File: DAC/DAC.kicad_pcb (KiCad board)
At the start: 4 copper layers, 54 x 21.6 mm, 32 parts, among them J1 Conn_01x06, J2 Conn_01x06, U1 TPS73633DBV, U2 PCM5242RHB

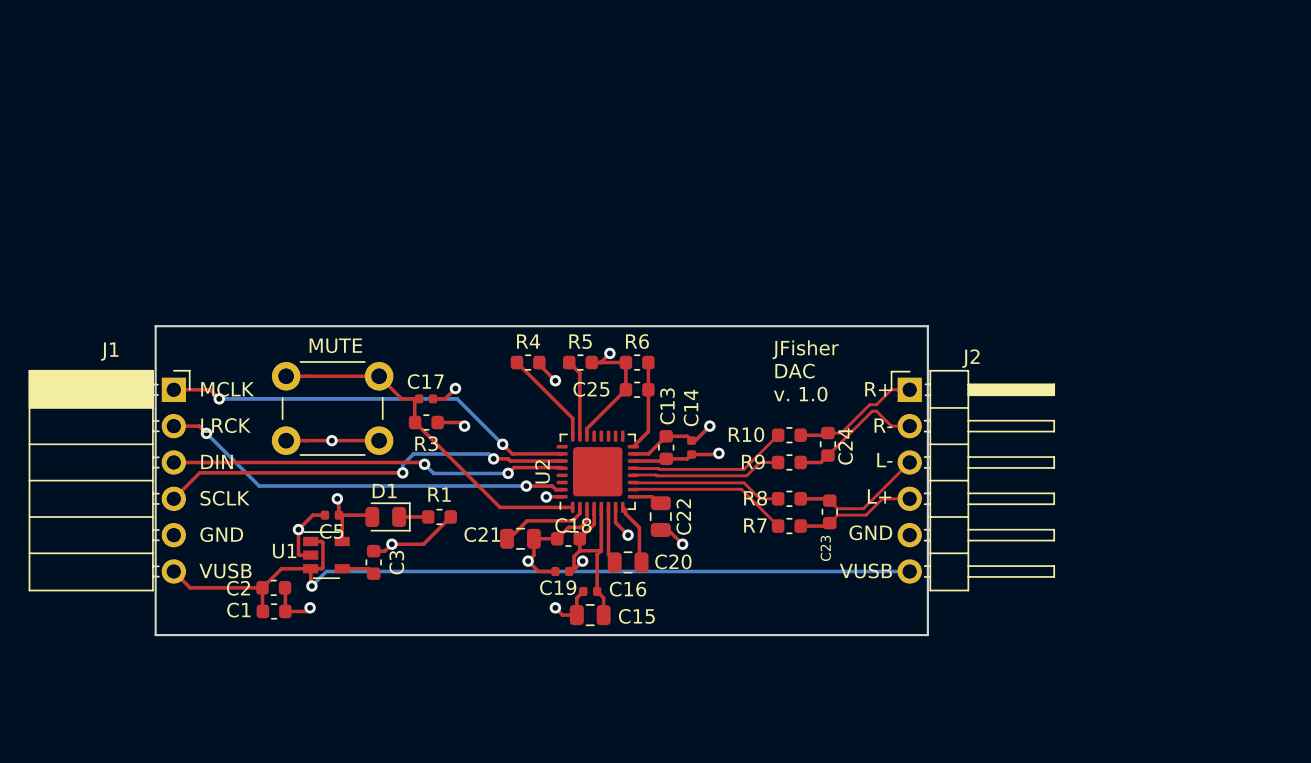
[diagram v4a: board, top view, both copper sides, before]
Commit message: Update DAC to expose config pins and to use larger components
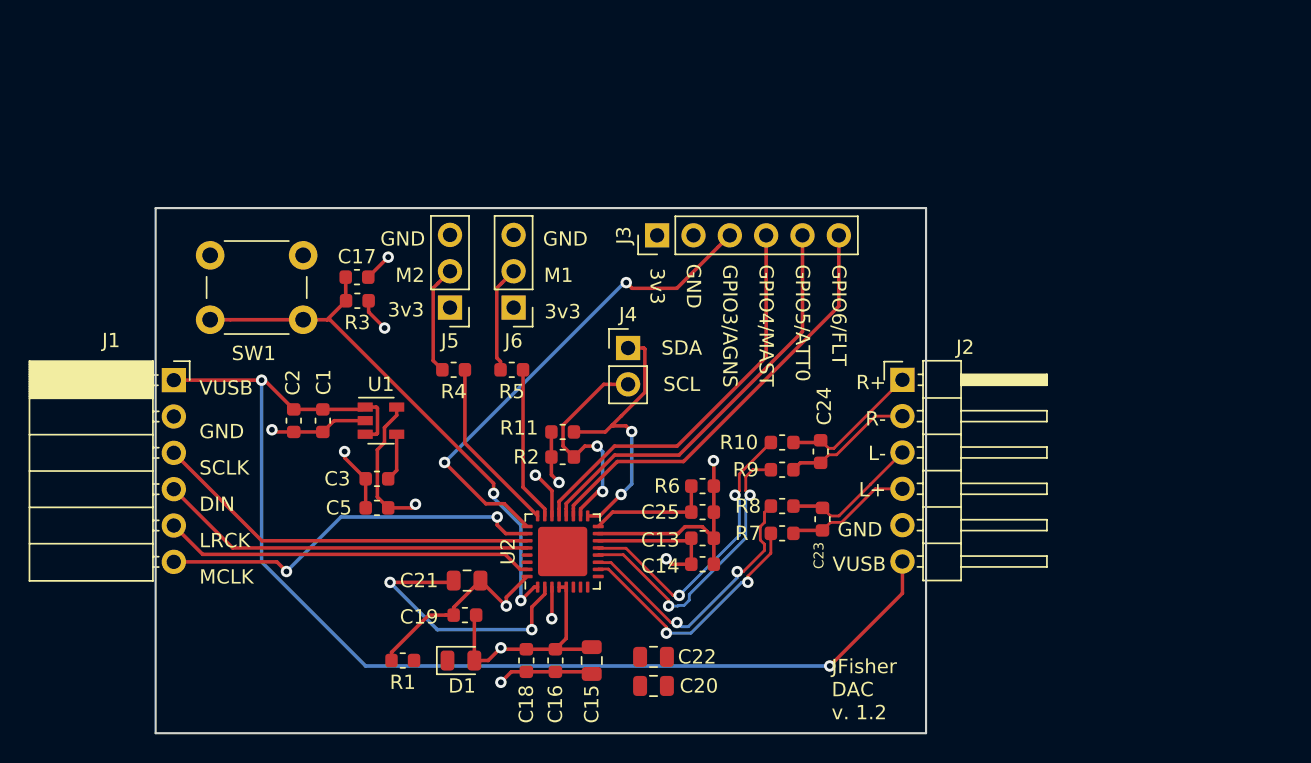
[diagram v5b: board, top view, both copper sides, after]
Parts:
- removed MUTE: SW_Push, Button_Switch_THT:SW_PUSH_6mm
- added J3: Conn_01x06_Male, Connector_PinHeader_2.54mm:PinHeader_1x06_P2.54mm_Vertical, F.Cu at (146.8, 34.3)
- added J4: Conn_01x02, Connector_PinHeader_2.54mm:PinHeader_1x02_P2.54mm_Vertical, F.Cu at (144.8, 42.2)
- added J5: Conn_01x03_Male, Connector_PinHeader_2.54mm:PinHeader_1x03_P2.54mm_Vertical, F.Cu at (132.3, 39.3)
- added J6: Conn_01x03_Male, Connector_PinHeader_2.54mm:PinHeader_1x03_P2.54mm_Vertical, F.Cu at (136.8, 39.3)
- added R11: 4.7k, Resistor_SMD:R_0603_1608Metric, F.Cu at (140.2, 48.0)
- added R2: 4.7k, Resistor_SMD:R_0603_1608Metric, F.Cu at (140.2, 49.8)
- added SW1: SW_Push, Button_Switch_THT:SW_PUSH_6mm, F.Cu at (115.6, 35.7)
- C14, C16, C17, C19, C5: footprint Capacitor_SMD:C_0402_1005Metric -> Capacitor_SMD:C_0603_1608Metric
- moved C1 13.8 mm to (123.4, 47.2), turned to 270 degrees
- moved C2 11.8 mm to (121.4, 47.2), turned to 270 degrees
- moved D1 11.3 mm to (133.1, 64.0), turned to 0 degrees
- moved R1 10.4 mm to (129.0, 64.0), turned to 180 degrees
- moved U1 10.1 mm to (127.5, 47.2)
- moved C22 9.82 mm to (146.6, 63.8), turned to 0 degrees
- moved C17 9.78 mm to (125.8, 37.2)
- moved R3 9.78 mm to (125.9, 38.9)
- moved R6 9.77 mm to (150.0, 51.8), turned to 180 degrees
- moved C25 9.70 mm to (150.0, 53.6), turned to 0 degrees
- moved C18 9.00 mm to (137.7, 64.0), turned to 270 degrees
- moved C20 8.82 mm to (146.6, 65.8)
- moved C14 8.19 mm to (150.0, 57.3), turned to 0 degrees
- moved C19 7.46 mm to (133.4, 60.8)
- moved C13 6.82 mm to (150.0, 55.5), turned to 0 degrees
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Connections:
- net Net-(R4-Pad1) renamed MODE2
- net Net-(R5-Pad1) renamed MODE1
- J1 pad 1: I2S_MCLK -> VUSB
- J1 pad 2: I2S_LRCK -> GND
- J1 pad 3: I2S_DIN -> I2S_SCLK
- J1 pad 4: I2S_SCLK -> I2S_DIN
- J1 pad 5: GND -> I2S_LRCK
- J1 pad 6: VUSB -> I2S_MCLK
- R4 pad 2: +3V3 -> Net-(J5-Pad2)
- R5 pad 2: GND -> Net-(J6-Pad2)
- U2 pad 17: (no net) -> SDA_MOSI_ATT2
- U2 pad 18: (no net) -> SCL_MC_ATT1
- U2 pad 19: (no net) -> GPIO5_ATT0
- U2 pad 20: (no net) -> GPIO4_MAST
- U2 pad 21: (no net) -> GPIO3_AGNS
- U2 pad 25: (no net) -> GPIO6_FLT
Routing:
- net GPIO6_FLT: track 0.00 -> 34.5 mm, vias 0 -> 2
- net GPIO5_ATT0: track 0.00 -> 30.0 mm
- net GPIO4_MAST: track 0.00 -> 29.1 mm
- net GPIO3_AGNS: track 0.00 -> 28.2 mm
- net VUSB: track 59.2 -> 82.7 mm, vias 1 -> 2
- net SDA_MOSI_ATT2: track 0.00 -> 19.5 mm, vias 0 -> 2
- net SCL_MC_ATT1: track 0.00 -> 16.1 mm, vias 0 -> 2
- net Net-(C17-Pad1): track 24.8 -> 38.6 mm, vias 0 -> 2
- net Net-(C21-Pad1): track 6.10 -> 19.1 mm, vias 0 -> 2
- net +3V3: track 30.9 -> 43.4 mm
- net OUTR_N: track 10.5 -> 20.7 mm, vias 0 -> 2
- net OUTR_P: track 11.1 -> 20.6 mm, vias 0 -> 2
- net OUTL_N: track 10.6 -> 19.5 mm, vias 0 -> 2
- net Net-(J5-Pad2): track 0.00 -> 7.64 mm
- net Net-(J6-Pad2): track 0.00 -> 7.48 mm
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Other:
- board size 54 x 21.6 mm -> 53.8 x 36.7 mm
- board text added: "3v3"
- board text added: "GPIO3/AGNS"
- board text added: "GPIO4/MAST"
- board text added: "GPIO5/ATT0"
- board text added: "GPIO6/FLT"
- board text added: "JFisher DAC v. 1.2"
- board text added: "M1"
- board text added: "M2"
- board text added: "SCL"
- board text added: "SDA"
- board text removed: "JFisher DAC v. 1.0"

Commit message: Update PCB placement
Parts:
- moved C22 3.44 mm to (149.9, 64.5)
- moved C20 1.60 mm to (145.6, 64.5)
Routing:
- net Net-(C22-Pad1): track 0.00 -> 9.07 mm
- net Net-(C20-Pad2): track 0.00 -> 7.78 mm
- net Net-(C20-Pad1): track 0.00 -> 7.17 mm
- net GND: track 56.2 -> 62.0 mm, vias 8 -> 10
- net Net-(D1-Pad1): track 0.00 -> 2.34 mm
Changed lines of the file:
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@@
     (thickness 1.6)
     (drawings 31)
-    (tracks 311)
+    (tracks 331)
     (zones 0)
     (modules 38)
@@
   )
   (module Capacitor_SMD:C_0805_2012Metric (layer F.Cu)
-    (at 146.558 65.786)
+    (at 145.5905 64.516)
     (descr "Capacitor SMD 0805 (2012 Metric), square (rectangular) end terminal, IPC_7351 nominal, (Body size source: https://docs.google.com/spreadsheets/d/1BsfQQcO9C6DZCsRaXUlFlo91Tg2WpOkGARC1WS5S8t0/edit?usp=sharing), generated with kicad-footprint-generator")
     (tags capacitor)
     (attr smd)
-    (fp_text reference C20 (at 3.175 0) (layer F.SilkS)
+    (fp_text reference C20 (at -0.0485 1.651) (layer F.SilkS)
       (effects (font (size 1 1) (thickness 0.15)))
     )
@@
   )
   (module Capacitor_SMD:C_0805_2012Metric (layer F.Cu)
-    (at 146.558 63.754)
+    (at 149.9085 64.516)
     (descr "Capacitor SMD 0805 (2012 Metric), square (rectangular) end terminal, IPC_7351 nominal, (Body size source: https://docs.google.com/spreadsheets/d/1BsfQQcO9C6DZCsRaXUlFlo91Tg2WpOkGARC1WS5S8t0/edit?usp=sharing), generated with kicad-footprint-generator")
     (tags capacitor)
     (attr smd)
-    (fp_text reference C22 (at 3.048 0) (layer F.SilkS)
+    (fp_text reference C22 (at 0.0785 1.651) (layer F.SilkS)
       (effects (font (size 1 1) (thickness 0.15)))
     )
@@
   (segment (start 139.458 53.9005) (end 139.458 52.139002) (width 0.25) (layer F.Cu) (net 5))
   (segment (start 139.458 52.139002) (end 138.372998 51.054) (width 0.25) (layer F.Cu) (net 5))
-  (segment (start 147.3455 63.604) (end 147.4955 63.754) (width 0.25) (layer F.Cu) (net 5))
   (segment (start 150.312888 54.995054) (end 150.7745 55.456666) (width 0.25) (layer F.Cu) (net 5))
   (segment (start 149.97449 54.656656) (end 150.312888 54.995054) (width 0.25) (layer F.Cu) (net 5))
@@
   (segment (start 150.7745 51.816) (end 150.7745 50.0635) (width 0.25) (layer F.Cu) (net 5))
   (segment (start 150.7745 50.0635) (end 150.749 50.038) (width 0.25) (layer F.Cu) (net 5))
+  (via (at 143.51 61.087) (size 0.8) (drill 0.4) (layers F.Cu B.Cu) (net 5))
+  (segment (start 143.182 61.087) (end 143.51 61.087) (width 0.25) (layer F.Cu) (net 5))
+  (segment (start 141.458 58.8755) (end 141.458 59.363) (width 0.25) (layer F.Cu) (net 5))
+  (segment (start 141.458 59.363) (end 143.182 61.087) (width 0.25) (layer F.Cu) (net 5))
+  (via (at 152.908 66.294) (size 0.8) (drill 0.4) (layers F.Cu B.Cu) (net 5))
+  (segment (start 150.846 64.516) (end 152.624 66.294) (width 0.25) (layer F.Cu) (net 5))
+  (segment (start 152.624 66.294) (end 152.908 66.294) (width 0.25) (layer F.Cu) (net 5))
   (segment (start 128.608 46.869) (end 128.608 46.294) (width 0.25) (layer F.Cu) (net 6))
   (segment (start 127.752999 47.724001) (end 128.608 46.869) (width 0.25) (layer F.Cu) (net 6))
@@
   (segment (start 135.382 51.627998) (end 123.941002 40.187) (width 0.25) (layer F.Cu) (net 7))
   (segment (start 135.382 52.324) (end 135.382 51.627998) (width 0.25) (layer F.Cu) (net 7))
+  (segment (start 129.8195 64.008) (end 132.1585 64.008) (width 0.25) (layer F.Cu) (net 8))
   (segment (start 158.8045 49.178) (end 159.1655 49.178) (width 0.2) (layer F.Cu) (net 9))
   (segment (start 158.242 48.6155) (end 158.8045 49.178) (width 0.2) (layer F.Cu) (net 9))
@@
   (segment (start 132.461 58.547) (end 132.588 58.42) (width 0.25) (layer F.Cu) (net 12))
   (segment (start 128.143 58.547) (end 132.461 58.547) (width 0.25) (layer F.Cu) (net 12))
+  (segment (start 144.096763 63.959763) (end 144.653 64.516) (width 0.25) (layer F.Cu) (net 13))
+  (segment (start 144.096763 63.422913) (end 144.096763 63.959763) (width 0.25) (layer F.Cu) (net 13))
+  (segment (start 140.958 60.28415) (end 144.096763 63.422913) (width 0.25) (layer F.Cu) (net 13))
+  (segment (start 140.958 58.8755) (end 140.958 60.28415) (width 0.25) (layer F.Cu) (net 13))
+  (segment (start 146.528 63.716) (end 146.528 64.516) (width 0.25) (layer F.Cu) (net 14))
+  (segment (start 146.528 63.031998) (end 146.528 63.716) (width 0.25) (layer F.Cu) (net 14))
+  (segment (start 143.858001 60.361999) (end 146.528 63.031998) (width 0.25) (layer F.Cu) (net 14))
+  (segment (start 143.444499 60.361999) (end 143.858001 60.361999) (width 0.25) (layer F.Cu) (net 14))
+  (segment (start 141.958 58.8755) (end 143.444499 60.361999) (width 0.25) (layer F.Cu) (net 14))
+  (segment (start 148.414763 63.959763) (end 148.971 64.516) (width 0.25) (layer F.Cu) (net 15))
+  (segment (start 148.250297 63.959763) (end 148.414763 63.959763) (width 0.25) (layer F.Cu) (net 15))
+  (segment (start 142.6955 58.404966) (end 148.250297 63.959763) (width 0.25) (layer F.Cu) (net 15))
+  (segment (start 142.6955 58.138) (end 142.6955 58.404966) (width 0.25) (layer F.Cu) (net 15))
   (via (at 120.904 57.785) (size 0.8) (drill 0.4) (layers F.Cu B.Cu) (net 16))
   (segment (start 113.03 57.1115) (end 120.2305 57.1115) (width 0.25) (layer F.Cu) (net 16))

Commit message: Add headers for MCLK/SCLK signal to allow for clock workaround
This helps to address the issue called out in the datasheet: https://e2e.ti.com/support/audio/f/6/p/804836/2980033#2980033, allowing the DAC to receive the MCLK input and create a usable SCLK input from it.
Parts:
- added J7: Conn_01x02, Connector_PinHeader_2.54mm:PinHeader_1x02_P2.54mm_Vertical, F.Cu at (126.0, 53.2)
- moved C3 7.98 mm to (119.5, 49.3), turned to 90 degrees
- moved U1 5.28 mm to (122.3, 48.1), turned to 270 degrees
- moved C5 4.82 mm to (126.7, 48.5), turned to 90 degrees
- moved C1 4.44 mm to (122.4, 42.9), turned to 0 degrees
- moved C2 2.75 mm to (122.5, 44.7), turned to 0 degrees
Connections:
- U2 pad 26: I2S_MCLK -> I2S_SCK_SRC
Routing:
- net I2S_MCLK: track 27.4 -> 16.4 mm
- net I2S_SCK_SRC: track 0.00 -> 9.99 mm
- net GND: track 62.0 -> 70.5 mm, vias 10 -> 8
- net VUSB: track 82.7 -> 86.1 mm
- net +3V3: track 43.4 -> 40.0 mm
- net Net-(C3-Pad1): track 3.36 -> 2.21 mm
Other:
- board text added: "I2S_MCLK"
- board text added: "SCK_SRC"
